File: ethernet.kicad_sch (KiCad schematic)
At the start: 116 parts, among them IC2 ACPL-217-500E, J2 5-2337992-8, U13 TPS2372-3RGWR, U16 TS3L500, U6 KSZ9031RNXCA, Y1 ABM8G-25.000MHZ-18-D2Y-T

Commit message: Rebase to Rev. 1.2.2
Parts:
- removed C119, C121, C123, C124, C132, C230: C_4u7_0402, data-center-dram-tester-footprints:0402-cap, symbol data-center-dram-tester:C_4u7_0402
- removed C120, C122, C125, C126, C127: C_470n_0402, data-center-dram-tester-footprints:0402-cap, symbol data-center-dram-tester:C_470n_0402
- removed C128, C221, C312: C_100n_0402, data-center-dram-tester-footprints:0402-cap, symbol data-center-dram-tester:C_100n_0402_16V
- removed C129, C131, C133, C134, C135, C136, C138, C139, C141, C142: C_10n_0402, data-center-dram-tester-footprints:0402-cap, symbol data-center-dram-tester:C_10n_0402
- removed C130: C_10n_0402, data-center-dram-tester-footprints:0402-cap, symbol data-center-dram-tester:C_470n_0402
- removed C137, C140: C_10n_0402, data-center-dram-tester-footprints:0402-cap, symbol data-center-dram-tester:C_4u7_0402
- removed C147, C148: C_22p_0402, data-center-dram-tester-footprints:0402-cap, symbol data-center-dram-tester:C_22p_0402
- removed C222: C_100n_0805_100V, data-center-dram-tester-footprints:0805-cap, symbol data-center-dram-tester:C_100n_0805_100V
- removed C223, C224, C225: C_22u_2220_100V, data-center-dram-tester-footprints:2220-cap, symbol data-center-dram-tester:C_22u_2220_100V
- removed C227, C228: C_47u_16V_1206, data-center-dram-tester-footprints:1206-cap, symbol data-center-dram-tester:C_47u_16V_1206
- removed C229, C287, C288, C289, C290, C291, C292, C293: C_100n_0402, antmicro-footprints:0402-cap, symbol antmicroCapacitors0402:C_100n_0402
- removed D12, D13: CD-MMBL110S, data-center-dram-tester-footprints:DFN3538, symbol data-center-dram-tester:CD-MMBL110S
- removed D14: PTVS58VS1UR,115, data-center-dram-tester-footprints:SOD-123F, symbol data-center-dram-tester:PTVS58VS1UR,115
- removed D15: KP-1608CGCK, data-center-dram-tester-footprints:LED_0603, symbol data-center-dram-tester:KP-1608CGCK
- removed D16: PDS760-13, data-center-dram-tester-footprints:PDS760-13, symbol data-center-dram-tester:PDS760-13
- removed FB1, FB2, FB3: BLM18PG121SN1D, data-center-dram-tester-footprints:0603-res, symbol data-center-dram-tester:BLM18PG121SN1D
- removed FB10, FB9: BLM21PG221SN1D, data-center-dram-tester-footprints:0805-res, symbol data-center-dram-tester:BLM21PG221SN1D
- removed IC2: ACPL-217-500E, data-center-dram-tester-footprints:SOIC127P700X242-4N, symbol data-center-dram-tester:ACPL-217-500E
- removed J2: 5-2337992-8, data-center-dram-tester-footprints:5-2337992-8, symbol data-center-dram-tester:5-2337992-8
- removed PS1: PDQE30-Q48-S12-D, data-center-dram-tester-footprints:PDQE30-Q48, symbol data-center-dram-tester:PDQE30-Q48-S12-D
- removed R100, R101, R102, R103, R104, R105, R106, R107, R108, R109, R110, R111, R112, R97, R98, R99: R_0R_0201, antmicro-footprints:0201-res, symbol antmicroResistorsmisc:R_0R_0201
- removed R156: R_1k3_0603, data-center-dram-tester-footprints:0603-res, symbol data-center-dram-tester:R_1k3_0603
- removed R159: R_49k9_0402, data-center-dram-tester-footprints:0402-res, symbol data-center-dram-tester:R_49k9_0402
- removed R161, R178, R179, R205, R206: R_0R_0402, antmicro-footprints:0402-res, symbol antmicroResistors0402:R_0R_0402
- removed R175: R_24k9_0402, data-center-dram-tester-footprints:0402-res, symbol data-center-dram-tester:R_24k9_0402
- removed R176, R85: R_63R4_0603, data-center-dram-tester-footprints:0603-res, symbol data-center-dram-tester:R_63R4_0603
- removed R177, R181, R182: R_10k_0402, data-center-dram-tester-footprints:0402-res, symbol data-center-dram-tester:R_10k_0402
- removed R180: R_32k4_0402, data-center-dram-tester-footprints:0402-res, symbol data-center-dram-tester:R_32k4_0402
- removed R183, R184: R_1k_0603, data-center-dram-tester-footprints:0603-res, symbol data-center-dram-tester:R_1k_0603
- removed R62, R67: R_220R_0402, data-center-dram-tester-footprints:0402-res, symbol data-center-dram-tester:R_220R_0402
- removed R68: R_12k1_0402, data-center-dram-tester-footprints:0402-res, symbol data-center-dram-tester:R_12k1_0402
- removed R69: R_1M8_0402, data-center-dram-tester-footprints:0402-res, symbol data-center-dram-tester:R_1M8_0402
- removed R70, R71, R72, R73, R74, R75, R76, R79, R80, R81: R_10k_0402, antmicro-footprints:0402-res, symbol antmicroResistors0402:R_10k_0402
- removed R77, R89, R90, R91, R92, R93, R94, R95, R96: R_2k2_0402, data-center-dram-tester-footprints:0402-res, symbol data-center-dram-tester:R_2k2_0402
- removed R78: R_1k_0402, data-center-dram-tester-footprints:0402-res, symbol data-center-dram-tester:R_1k_0402
- removed U13: TPS2372-3RGWR, antmicro-footprints:Texas_RGW0020B, symbol antmicroPMICPowerDistributionSwitchesLoadDrivers:TPS2372-3RGWR
- removed U16: TS3L500, antmicro-footprints:Texas_RHU0056A, symbol antmicroLogicSignalSwitchesMultiplexersDecoders:TS3L500
- removed U6: KSZ9031RNXCA, data-center-dram-tester-footprints:QFN-48-Microchip-QFN77-48LD-PL-2, symbol data-center-dram-tester:KSZ9031RNXCA
- removed Y1: ABM8G-25.000MHZ-18-D2Y-T, data-center-dram-tester-footprints:KX-7, symbol data-center-dram-tester:ABM8G-25.000MHZ-18-D2Y-T
- added C119, C121, C123, C124, C132, C137, C140, C230: C_4u7_0402, data-center-rdimm-ddr4-tester-footprints:C_0402_1005Metric, symbol data-center-rdimm-ddr4-tester:C_4u7_0402
- added C120, C122, C125, C126, C127, C130: C_470n_0402, data-center-rdimm-ddr4-tester-footprints:C_0402_1005Metric, symbol data-center-rdimm-ddr4-tester:C_470n_0402
- added C128, C221, C312: C_100n_16V_0402, data-center-rdimm-ddr4-tester-footprints:C_0402_1005Metric, symbol data-center-rdimm-ddr4-tester:C_100n_16V_0402
- added C129, C131, C133, C134, C135, C136, C138, C139, C141, C142: C_10n_0402, data-center-rdimm-ddr4-tester-footprints:C_0402_1005Metric, symbol data-center-rdimm-ddr4-tester:C_10n_0402
- added C147, C148: C_22p_0402, data-center-rdimm-ddr4-tester-footprints:C_0402_1005Metric, symbol data-center-rdimm-ddr4-tester:C_22p_0402
- added C222: C_100n_0805_100V, data-center-rdimm-ddr4-tester-footprints:C_0805_2012Metric, symbol data-center-rdimm-ddr4-tester:C_100n_0805_100V
- added C223, C224, C225: C_22u_100V_2220, data-center-rdimm-ddr4-tester-footprints:C_2220_5650Metric, symbol data-center-rdimm-ddr4-tester:C_22u_100V_2220
- added C227, C228: C_47u_16V_1206, data-center-rdimm-ddr4-tester-footprints:C_1206_3216Metric, symbol data-center-rdimm-ddr4-tester:C_47u_16V_1206
- added C229, C287, C288, C289, C290, C291, C292, C293: C_100n_0402, data-center-rdimm-ddr4-tester-footprints:C_0402_1005Metric, symbol data-center-rdimm-ddr4-tester:C_100n_0402
- added D12, D13: CD-MMBL110S, data-center-rdimm-ddr4-tester-footprints:DFN3538, symbol data-center-rdimm-ddr4-tester:CD-MMBL110S
- added D14: PTVS58VS1UR,115, data-center-rdimm-ddr4-tester-footprints:SOD-123F, symbol data-center-rdimm-ddr4-tester:PTVS58VS1UR,115
- added D15: LED_G_0603_KP-1608CGCK, data-center-rdimm-ddr4-tester-footprints:LED_0603_1608Metric_G, symbol data-center-rdimm-ddr4-tester:LED_G_0603_KP-1608CGCK
- added D16: PDS760, data-center-rdimm-ddr4-tester-footprints:PowerDI5, symbol data-center-rdimm-ddr4-tester:PDS760
- added FB1, FB2, FB3: FB_120Z_2A_0603, data-center-rdimm-ddr4-tester-footprints:FB_0603_1608Metric, symbol data-center-rdimm-ddr4-tester:FB_120Z_2A_0603
- added FB10, FB9: FB_220Z_2A_0603, data-center-rdimm-ddr4-tester-footprints:FB_0805_2012Metric, symbol data-center-rdimm-ddr4-tester:FB_220Z_2A_0603
- added IC2: ACPL-217-500E, data-center-rdimm-ddr4-tester-footprints:SOIC-4_4.55x2.6mm_P1.27, symbol data-center-rdimm-ddr4-tester:ACPL-217-500E
- added J2: Bus_RJ45_5-2337992-8, data-center-rdimm-ddr4-tester-footprints:RJ45_5-2337992-8_Horizontal, symbol data-center-rdimm-ddr4-tester:Bus_RJ45_5-2337992-8
- added PS1: PDQE30-Q48-S12-D, data-center-rdimm-ddr4-tester-footprints:CONV_PDQE30-Q48-S5-D, symbol data-center-rdimm-ddr4-tester:PDQE30-Q48-S12-D
- added R100, R101, R102, R103, R104, R105, R106, R107, R108, R109, R110, R111, R112, R221, R222, R97, R98, R99: R_0R_0201, data-center-rdimm-ddr4-tester-footprints:R_0201, symbol data-center-rdimm-ddr4-tester:R_0R_0201
- added R156: R_1k3_0603, data-center-rdimm-ddr4-tester-footprints:R_0603_1608Metric, symbol data-center-rdimm-ddr4-tester:R_1k3_0603
- added R159: R_49k9_0402, data-center-rdimm-ddr4-tester-footprints:R_0402_1005Metric, symbol data-center-rdimm-ddr4-tester:R_49k9_0402
- added R161, R178, R179, R205, R206: R_0R_0402, data-center-rdimm-ddr4-tester-footprints:R_0402_1005Metric, symbol data-center-rdimm-ddr4-tester:R_0R_0402
- added R175: R_24k9_0402, data-center-rdimm-ddr4-tester-footprints:R_0402_1005Metric, symbol data-center-rdimm-ddr4-tester:R_24k9_0402
- added R176, R85: R_63R4_0603, data-center-rdimm-ddr4-tester-footprints:R_0603_1608Metric, symbol data-center-rdimm-ddr4-tester:R_63R4_0603
- added R177, R181, R182, R70, R71, R72, R73, R74, R75, R76, R79, R80, R81: R_10k_0402, data-center-rdimm-ddr4-tester-footprints:R_0402_1005Metric, symbol data-center-rdimm-ddr4-tester:R_10k_0402
- added R180: R_32k4_0402, data-center-rdimm-ddr4-tester-footprints:R_0402_1005Metric, symbol data-center-rdimm-ddr4-tester:R_32k4_0402
- added R183, R184: R_1k_0603, data-center-rdimm-ddr4-tester-footprints:R_0603_1608Metric, symbol data-center-rdimm-ddr4-tester:R_1k_0603
- added R62, R67: R_220R_0402, data-center-rdimm-ddr4-tester-footprints:R_0402_1005Metric, symbol data-center-rdimm-ddr4-tester:R_220R_0402
- added R68: R_12k1_0402, data-center-rdimm-ddr4-tester-footprints:R_0402_1005Metric, symbol data-center-rdimm-ddr4-tester:R_12k1_0402
- added R69: R_1M8_0402, data-center-rdimm-ddr4-tester-footprints:R_0402_1005Metric, symbol data-center-rdimm-ddr4-tester:R_1M8_0402
- added R77, R89, R90, R91, R92, R93, R94, R95, R96: R_2k2_0402, data-center-rdimm-ddr4-tester-footprints:R_0402_1005Metric, symbol data-center-rdimm-ddr4-tester:R_2k2_0402
- added R78: R_1k_0402, data-center-rdimm-ddr4-tester-footprints:R_0402_1005Metric, symbol data-center-rdimm-ddr4-tester:R_1k_0402
- added U13: TPS2372-3RGWR, data-center-rdimm-ddr4-tester-footprints:VQFN-20_5x5x1mm_P0.65mm, symbol data-center-rdimm-ddr4-tester:TPS2372-3RGWR
- added U16: TS3L500RHUR, data-center-rdimm-ddr4-tester-footprints:WQFN-56-1EP_5x11x1mm_P0.5mm, symbol data-center-rdimm-ddr4-tester:TS3L500RHUR
- added U6: KSZ9031RNXCA, data-center-rdimm-ddr4-tester-footprints:QFN-48-1EP_7x7x0.9mm_P0.5mm_EP3.5x3.5mm, symbol data-center-rdimm-ddr4-tester:KSZ9031RNXCA
- added Y1: Oscillator_SMD_25MHz_KX-7, data-center-rdimm-ddr4-tester-footprints:Oscillator_SMD_Geyer_KX-7-4Pin_3.2x2.5mm, symbol data-center-rdimm-ddr4-tester:Oscillator_SMD_25MHz_KX-7
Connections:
- net 1V2_SYS: now also C119.1, C120.1, C122.1, C126.1, C130.1, C135.1, C138.1, C141.1, C142.1, FB2.2, FB3.2, U6.14 (DVDDL), U6.18 (DVDDL), U6.23 (DVDDL), U6.26 (DVDDL), U6.30 (DVDDL), U6.39 (DVDDL)
- net AMPS_CTL: now also R156.2, U13.8 (AMPS_CTL)
- net AVDDH: now also C132.1, C137.1, C140.1, FB1.2, U6.1 (AVDDH), U6.12 (AVDDH)
- net AVDDL: now also C121.1, C125.1, C129.1, C134.1, FB3.1, U6.4 (AVDDL), U6.9 (AVDDL)
- net AVDDL_PLL: now also C124.2, C128.2, C133.2, FB2.1, U6.44 (AVDDL_PLL)
- net CLSA: now also R85.2, U13.3 (CLSA)
- net CLSB: now also R176.2, U13.6 (CLSB)
- net DEN: now also R175.1, U13.2 (DEN)
- net ETH1_BP_N: now also R106.2, R98.1
- net ETH1_BP_P: now also R105.1, R97.2
- net ETH1_N: now also R98.2, U16.3 (A1), U6.3 (TXRXM_A)
- net ETH1_P: now also R97.1, U16.2 (A0), U6.2 (TXRXP_A)
- net ETH2_BP_N: now also R100.1, R108.2
- net ETH2_BP_P: now also R107.1, R99.2
- net ETH2_N: now also R100.2, U16.8 (A3), U6.6 (TXRXM_B)
- net ETH2_P: now also R99.1, U16.7 (A2), U6.5 (TXRXP_B)
- net ETH3_BP_N: now also R102.1, R110.2
- net ETH3_BP_P: now also R101.2, R109.1
- net ETH3_N: now also R102.2, U16.12 (A5), U6.8 (TXRXM_C)
- net ETH3_P: now also R101.1, U16.11 (A4), U6.7 (TXRXP_C)
- net ETH4_BP_N: now also R104.1, R112.2
- net ETH4_BP_P: now also R103.2, R111.1
- net ETH4_N: now also R104.2, U16.15 (A7), U6.11 (TXRXM_D)
- net ETH4_P: now also R103.1, U16.14 (A6), U6.10 (TXRXP_D)
- net ETH_INT_N: now also U6.38 (~{INT/PME})
- net ETH_MDC: now also U6.36 (MDC)
- net ETH_MDIO: now also R78.1, U6.37 (MDIO)
- net ETH_REF_CLK: now also R76.1, R94.1, U6.41 (CLK125_NDO/LED_MODE)
- net ETH_RSTN: now also R79.1, U6.42 (~{RESET})
- net ETH_RXD0: now also R70.1, R77.1, U6.32 (RXD0/MODE0)
- net ETH_RXD1: now also R71.1, R89.1, U6.31 (RXD1/MODE1)
- net ETH_RXD2: now also R72.1, R90.1, U6.28 (RXD2/MODE2)
- net ETH_RXD3: now also R73.1, R91.1, U6.27 (RXD3/MODE3)
- net ETH_RX_CLK: now also R75.1, R93.1, U6.35 (RX_CLK/PHYAD2)
- net ETH_RX_DV: now also R74.1, R92.1, U6.33 (RX_DV/CLK125_EN)
- net ETH_SEL: now also R206.1
- net ETH_TXD0: now also U6.19 (TXD0)
- net ETH_TXD1: now also U6.20 (TXD1)
- net ETH_TXD2: now also U6.21 (TXD2)
- net ETH_TXD3: now also U6.22 (TXD3)
- net ETH_TX_CLK: now also U6.24 (GTX_CLK)
- net ETH_TX_EN: now also U6.25 (TX_EN)
- net EXT_ETH1_N: now also U16.47 (1B1)
- net EXT_ETH1_P: now also U16.48 (0B1)
- net EXT_ETH2_N: now also U16.42 (3B1)
- net EXT_ETH2_P: now also U16.43 (2B1)
- net EXT_ETH3_N: now also U16.36 (5B1)
- net EXT_ETH3_P: now also U16.37 (4B1)
- net EXT_ETH4_N: now also U16.31 (7B1)
- net EXT_ETH4_P: now also U16.32 (6B1)
- net EXT_LED_LINK: now also U16.23 (1LED1)
- net EXT_LED_SPD: now also U16.52 (2LED1)
- net GND: now also C119.2, C120.2, C121.2, C122.2, C123.2, C124.1, C125.2, C126.2, C127.2, C128.1, C129.2, C130.2, C131.2, C132.2, C133.1, C134.2, C135.2, C136.2, C137.2, C138.2, C139.2, C140.2, C141.2, C142.2, C147.2, C148.2, C221.2, C227.2, C228.2, C229.2, C230.2, C287.2, C288.2, C289.2, C290.2, C291.2, C292.2, C293.2, C312.2, PS1.6 (GND), R184.2, R68.1, R77.2, R89.2, R90.2, R91.2, R92.2, R93.2, R94.2, R95.2, R96.2, U16.1 (GND), U16.13 (GND), U16.16 (GND), U16.19 (LED0), U16.21 (GND), U16.24 (GND), U16.28 (GND), U16.33 (GND), U16.39 (GND), U16.44 (GND), U16.49 (GND), U16.53 (GND), U16.55 (GND), U16.57 (EP), U16.6 (GND), U16.9 (GND), U6.29 (VSS), U6.49 (PAD_GND), Y1.2 (SH), Y1.4 (SH)
- net GNDD: now also C223.2, C224.2, C225.2, D15.2, PS1.2 (VIN-), R179.1, R183.1, U13.11 (RTNA), U13.12 (RTNB)
- net GNDS: now also J2.19 (SHIELD), J2.20 (SHIELD)
- net INT_ETH1_N: now also J2.2 (P2), R106.1, U16.45 (1B2)
- net INT_ETH1_P: now also J2.1 (P1), R105.2, U16.46 (0B2)
- net INT_ETH2_N: now also J2.6 (P6), R108.1, U16.40 (3B2)
- net INT_ETH2_P: now also J2.3 (P3), R107.2, U16.41 (2B2)
- net INT_ETH3_N: now also J2.8 (P8), R110.1, U16.34 (5B2)
- net INT_ETH3_P: now also J2.7 (P7), R109.2, U16.35 (4B2)
- net INT_ETH4_N: now also J2.10 (P10), R112.1, U16.29 (7B2)
- net INT_ETH4_P: now also J2.9 (P9), R111.2, U16.30 (6B2)
- net INT_LED_LINK: now also J2.18 (LED_YEL-), R221.2, U16.26 (1LED2)
- net INT_LED_SPD: now also J2.16 (LED_GRN-), R222.2, U16.51 (2LED2)
- net IRSHDL_EN: now also R179.2, U13.16 (IRSHDL_EN)
- net LED_LINK: now also R221.1, R81.1, R96.1, U16.20 (LED1), U6.17 (LED1/PHAD0/PME_N1)
- net LED_SPD: now also R222.1, R80.1, R95.1, U16.54 (LED2), U6.15 (LED2/PHYAD1)
- net MPS_DUTY: now also R161.2, U13.9 (MPS_DUTY)
- net PAIR_12: now also D12.4, J2.11 (VC1)
- net PAIR_36: now also D12.3, J2.12 (VC2)
- net PAIR_78: now also D13.3, J2.13 (VC3)
- net PAIR_910: now also D13.4, J2.14 (VC4)
- net PG: now also R178.1, U13.13 (PG)
- net POE_ACTIVE: now also IC2.4, PS1.1 (CTRL), R178.2
- net PRSNT_M2C: now also R205.1
- net REF: now also R159.2, U13.7 (REF)
- net TPH: now also R177.1, U13.18 (TPH)
- net TPL: now also R181.1, U13.17 (TPL)
- net VDD: now also C222.1, C223.1, C224.1, C225.1, D14.K (C), FB9.2, PS1.3 (VIN+), R175.2, R177.2, R180.2, R181.2, R182.2, U13.1 (VDD)
- net VDD_RAW: now also D12.2, D13.2, FB9.1
- net VIN: now also D16.C
- net VIN_POE: now also C227.1, C228.1, C229.1, D16.A, PS1.4 (VOUT)
- net VIN_RAW: now also IC2.1
- net VSS: now also C222.2, D14.A, FB10.2, R156.1, R159.1, R161.1, R176.1, R85.1, U13.21 (PAD_VSSC), U13.4 (VSSA), U13.5 (VSSB)
- net VSS_RAW: now also D12.1, D13.1, FB10.1
- new net: C147.1, R69.1, U6.45 (XO), Y1.1
- new net: C148.1, R69.2, U6.46 (XI), Y1.3
- new net: U6.13 (NC), U6.47 (NC)
- new net: R68.2, U6.48 (ISET)
- new net: J2.17 (LED_YEL+), R62.1
- new net: J2.15 (LED_GRN+), R67.1
- new net: R205.2, R206.2, U16.17 (SEL)
- new net: D15.1, R180.1
- new net: R182.1, U13.19 (~{BT})
- new net: IC2.2, R184.1
- new net: IC2.3, R183.2
- new net: C312.1, J2.5 (P5)
- new net: C221.1, J2.4 (P4)
- new net 3V3_SYS: C123.1, C127.1, C131.1, C136.1, C139.1, C230.1, C287.1, C288.1, C289.1, C290.1, C291.1, C292.1, C293.1, FB1.1, R62.2, R67.2, R70.2, R71.2, R72.2, R73.2, R74.2, R75.2, R76.2, R78.2, R79.2, R80.2, R81.2, U16.10 (VCC), U16.18 (VCC), U16.27 (VCC), U16.38 (VCC), U16.4 (VCC), U16.50 (VCC), U16.56 (VCC), U6.16 (DVDDH), U6.34 (DVDDH), U6.40 (DVDDH)
- no-connect marks 4 -> 5
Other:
- note added: "Do not use mux with PoE"
- note added: "Use when ETH on FMC is needed"

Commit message: Remove PoE and ETH mux
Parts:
- removed C222: C_100n_0805_100V, data-center-rdimm-ddr4-tester-footprints:C_0805_2012Metric, symbol data-center-rdimm-ddr4-tester:C_100n_0805_100V
- removed C223, C224, C225: C_22u_100V_2220, data-center-rdimm-ddr4-tester-footprints:C_2220_5650Metric, symbol data-center-rdimm-ddr4-tester:C_22u_100V_2220
- removed C227, C228: C_47u_16V_1206, data-center-rdimm-ddr4-tester-footprints:C_1206_3216Metric, symbol data-center-rdimm-ddr4-tester:C_47u_16V_1206
- removed C229, C287, C288, C289, C290, C291, C292, C293: C_100n_0402, data-center-rdimm-ddr4-tester-footprints:C_0402_1005Metric, symbol data-center-rdimm-ddr4-tester:C_100n_0402
- removed C230: C_4u7_0402, data-center-rdimm-ddr4-tester-footprints:C_0402_1005Metric, symbol data-center-rdimm-ddr4-tester:C_4u7_0402
- removed D12, D13: CD-MMBL110S, data-center-rdimm-ddr4-tester-footprints:DFN3538, symbol data-center-rdimm-ddr4-tester:CD-MMBL110S
- removed D14: PTVS58VS1UR,115, data-center-rdimm-ddr4-tester-footprints:SOD-123F, symbol data-center-rdimm-ddr4-tester:PTVS58VS1UR,115
- removed D15: LED_G_0603_KP-1608CGCK, data-center-rdimm-ddr4-tester-footprints:LED_0603_1608Metric_G, symbol data-center-rdimm-ddr4-tester:LED_G_0603_KP-1608CGCK
- removed D16: PDS760, data-center-rdimm-ddr4-tester-footprints:PowerDI5, symbol data-center-rdimm-ddr4-tester:PDS760
- removed FB10, FB9: FB_220Z_2A_0603, data-center-rdimm-ddr4-tester-footprints:FB_0805_2012Metric, symbol data-center-rdimm-ddr4-tester:FB_220Z_2A_0603
- removed IC2: ACPL-217-500E, data-center-rdimm-ddr4-tester-footprints:SOIC-4_4.55x2.6mm_P1.27, symbol data-center-rdimm-ddr4-tester:ACPL-217-500E
- removed PS1: PDQE30-Q48-S12-D, data-center-rdimm-ddr4-tester-footprints:CONV_PDQE30-Q48-S5-D, symbol data-center-rdimm-ddr4-tester:PDQE30-Q48-S12-D
- removed R100, R101, R102, R103, R104, R105, R106, R107, R108, R109, R110, R111, R112, R221, R222, R97, R98, R99: R_0R_0201, data-center-rdimm-ddr4-tester-footprints:R_0201, symbol data-center-rdimm-ddr4-tester:R_0R_0201
- removed R156: R_1k3_0603, data-center-rdimm-ddr4-tester-footprints:R_0603_1608Metric, symbol data-center-rdimm-ddr4-tester:R_1k3_0603
- removed R159: R_49k9_0402, data-center-rdimm-ddr4-tester-footprints:R_0402_1005Metric, symbol data-center-rdimm-ddr4-tester:R_49k9_0402
- removed R161, R178, R179, R205, R206: R_0R_0402, data-center-rdimm-ddr4-tester-footprints:R_0402_1005Metric, symbol data-center-rdimm-ddr4-tester:R_0R_0402
- removed R175: R_24k9_0402, data-center-rdimm-ddr4-tester-footprints:R_0402_1005Metric, symbol data-center-rdimm-ddr4-tester:R_24k9_0402
- removed R176, R85: R_63R4_0603, data-center-rdimm-ddr4-tester-footprints:R_0603_1608Metric, symbol data-center-rdimm-ddr4-tester:R_63R4_0603
- removed R177, R181, R182: R_10k_0402, data-center-rdimm-ddr4-tester-footprints:R_0402_1005Metric, symbol data-center-rdimm-ddr4-tester:R_10k_0402
- removed R180: R_32k4_0402, data-center-rdimm-ddr4-tester-footprints:R_0402_1005Metric, symbol data-center-rdimm-ddr4-tester:R_32k4_0402
- removed R183, R184: R_1k_0603, data-center-rdimm-ddr4-tester-footprints:R_0603_1608Metric, symbol data-center-rdimm-ddr4-tester:R_1k_0603
- removed U13: TPS2372-3RGWR, data-center-rdimm-ddr4-tester-footprints:VQFN-20_5x5x1mm_P0.65mm, symbol data-center-rdimm-ddr4-tester:TPS2372-3RGWR
- removed U16: TS3L500RHUR, data-center-rdimm-ddr4-tester-footprints:WQFN-56-1EP_5x11x1mm_P0.5mm, symbol data-center-rdimm-ddr4-tester:TS3L500RHUR
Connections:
- net INT_ETH1_N is gone; now on net ETH1_N: J2.2 (P2)
- net INT_ETH1_P is gone; now on net ETH1_P: J2.1 (P1)
- net INT_ETH2_N is gone; now on net ETH2_N: J2.6 (P6)
- net INT_ETH2_P is gone; now on net ETH2_P: J2.3 (P3)
- net INT_ETH3_N is gone; now on net ETH3_N: J2.8 (P8)
- net INT_ETH3_P is gone; now on net ETH3_P: J2.7 (P7)
- net INT_ETH4_N is gone; now on net ETH4_N: J2.10 (P10)
- net INT_ETH4_P is gone; now on net ETH4_P: J2.9 (P9)
- net INT_LED_LINK is gone; now on net LED_LINK: J2.18 (LED_YEL-)
- net INT_LED_SPD is gone; now on net LED_SPD: J2.16 (LED_GRN-)
- no-connect marks 5 -> 1
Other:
- note removed: "Do not use mux with PoE"
- note removed: "ETH mux"
- note removed: "PoE"
- note removed: "Stubless mux passthrough"
- note removed: "Use when ETH on FMC is needed"

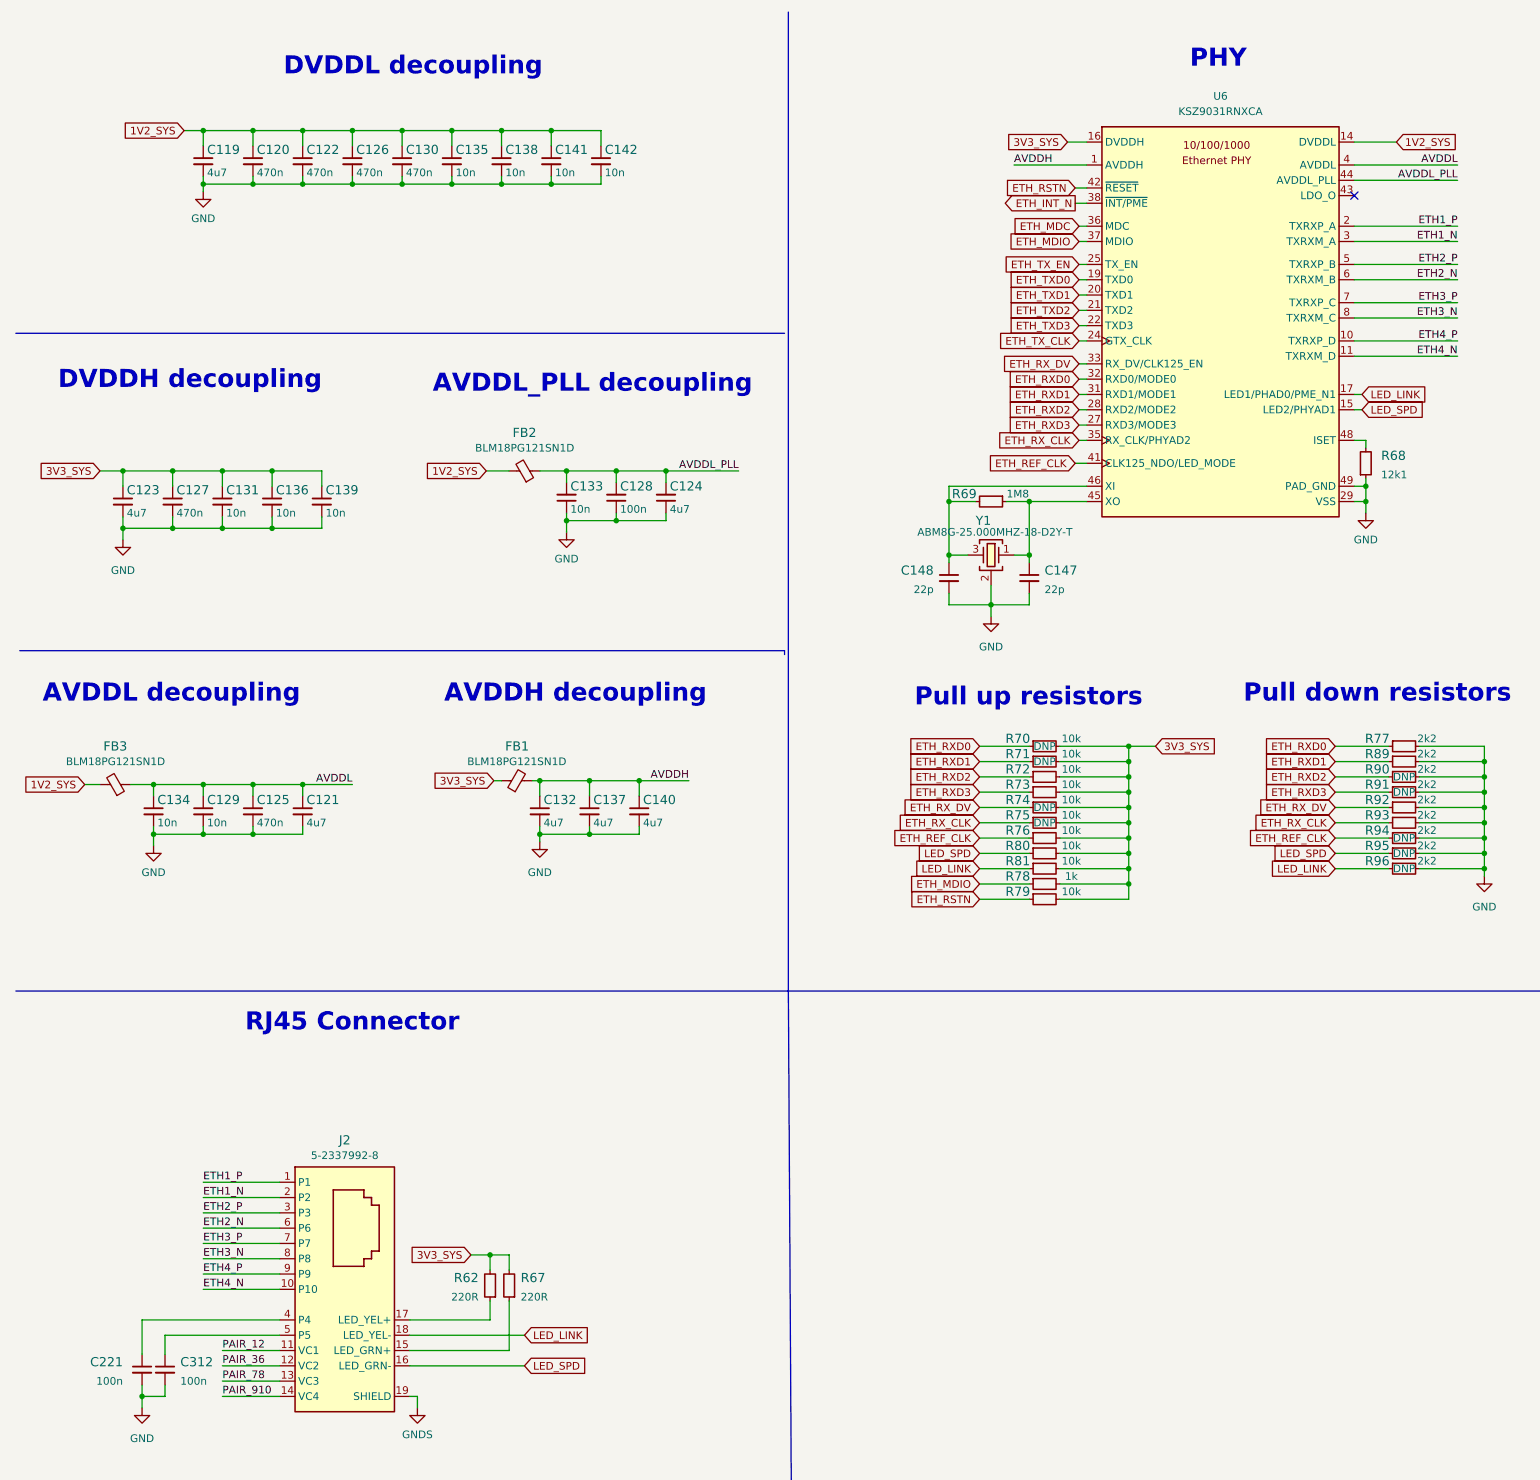
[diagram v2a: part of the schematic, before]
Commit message: Update designators and sync schematic with PCB
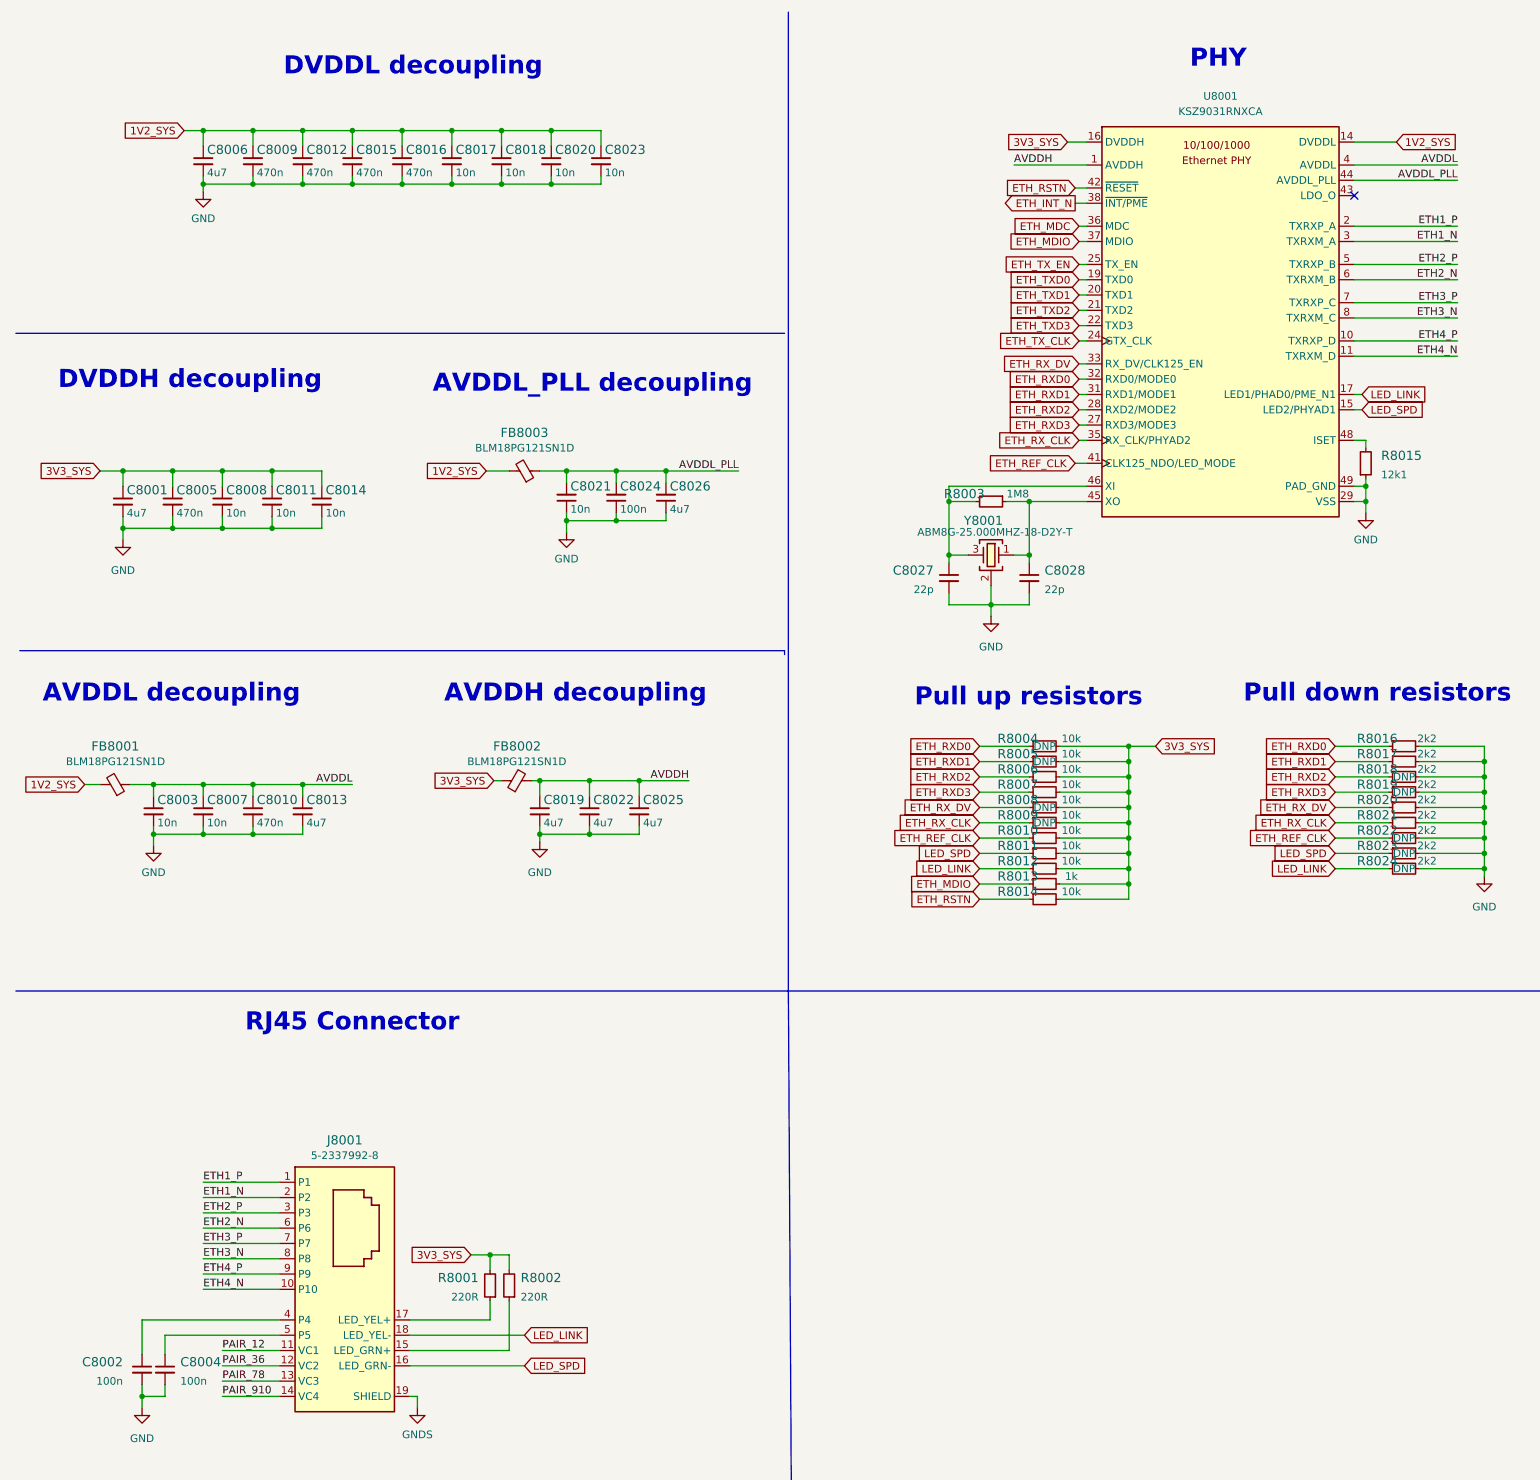
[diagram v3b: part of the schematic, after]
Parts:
- renumbered C123 to C8001, C221 to C8002, C134 to C8003, C312 to C8004, C127 to C8005, C119 to C8006, C129 to C8007, C131 to C8008, C120 to C8009, C125 to C8010, C136 to C8011, C122 to C8012, C121 to C8013, C139 to C8014, C126 to C8015, C130 to C8016, C135 to C8017, C138 to C8018, C132 to C8019, C141 to C8020, C133 to C8021, C137 to C8022, C142 to C8023, C128 to C8024, C140 to C8025, C124 to C8026, C148 to C8027, C147 to C8028, FB3 to FB8001, FB1 to FB8002, FB2 to FB8003, J2 to J8001, R62 to R8001, R67 to R8002, R69 to R8003, R70 to R8004, R71 to R8005, R72 to R8006, R73 to R8007, R74 to R8008, R75 to R8009, R76 to R8010, R80 to R8011, R81 to R8012, R78 to R8013, R79 to R8014, R68 to R8015, R77 to R8016, R89 to R8017, R90 to R8018, R91 to R8019, R92 to R8020, R93 to R8021, R94 to R8022, R95 to R8023, R96 to R8024, U6 to U8001, Y1 to Y8001
